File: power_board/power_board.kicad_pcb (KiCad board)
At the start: 2 copper layers, 165.3 x 121.3 mm, 67 parts, among them J1 PROG, J10 M4, J11 5V_1, J12 M5, J13 M6, J14 M7, J15 FAN, J16 Screw_Terminal_01x02, J17 MB_interface, J18 Conn_01x02_Female, J19 12V_1, J2 M1, J20 12V_2, J21 12V_3, J22 12V_4, J23 48V_1, J24 48V_2, J25 48V_3, J26 48V_4, J3 M2, J4 Conn_01x02_Female, J5 Conn_01x02_Female, J6 Conn_01x01_Male, J7 Conn_01x01_Male, J8 Screw_Terminal_01x02, J9 M3, Q1 2N3906, SW1 SW_Push, U1 ACS758xCB-050B-PFF, U2 ACS758xCB-050B-PFF, U3 MCP2515-EST, U4 MAX31855KASA, U5 MCP2551-I-SN, U6 BTS50085-1TMA, U7 ATmega328P-AU, U8 BTS50085-1TMA, U9 LM2596S-5, Y1 20Mhz, Y2 16Mhz

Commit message: silkscreen
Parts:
- added G***: LOGO, title:title, F.Cu at (157.0, 104.5)
- added G***: LOGO, logo:logo, F.Cu at (113.3, 99.8)
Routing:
- net GNDREF: vias 119 -> 118
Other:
- board text added: "- +"
- board text added: "12V-1"
- board text added: "48V-1"
- board text added: "48V-2"
- board text added: "48V-3"
- board text added: "48V-4"
- board text added: "Fan"
- board text added: "M3"
- board text added: "M6"
- board text added: "Motor 1"
- board text added: "Motor 2"
- board text added: "Motor 4"
- board text added: "Motor 5"
- board text added: "Motor 7"
- board text added: "POWER BOARD - REV 1.0"

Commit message: finishing silkscreen
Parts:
- moved R9 1.27 mm to (213.8, 93.6)
- moved C14 0.38 mm to (221.6, 52.5)
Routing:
- net Net-(R9-Pad2): track 1.75 -> 2.49 mm
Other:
- board text added: "12V-2"
- board text added: "12V-3"
- board text added: "12V-4"
- board text added: "5V"
- board text added: "CH"
- board text added: "CL"
- board text added: "Leak Sensors"
- board text added: "TC"
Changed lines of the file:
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@@
   (general
     (thickness 1.6)
-    (drawings 679)
-    (tracks 756)
+    (drawings 688)
+    (tracks 758)
     (zones 0)
     (modules 69)
@@
     (44 Edge.Cuts user)
     (45 Margin user)
-    (46 B.CrtYd user)
-    (47 F.CrtYd user)
+    (46 B.CrtYd user hide)
+    (47 F.CrtYd user hide)
     (48 B.Fab user hide)
     (49 F.Fab user hide)
@@
     (tags resistor)
     (attr smd)
-    (fp_text reference R14 (at 0 1.524 180) (layer F.SilkS)
+    (fp_text reference R14 (at 1.1175 -1.651 180) (layer F.SilkS)
       (effects (font (size 1 1) (thickness 0.15)))
     )
@@
   )
   (module Capacitor_THT:CP_Radial_D7.5mm_P2.50mm (layer F.Cu)
-    (at 221.234 52.451 270)
+    (at 221.615 52.451 270)
     (descr "CP, Radial series, Radial, pin pitch=2.50mm, , diameter=7.5mm, Electrolytic Capacitor")
     (tags "CP Radial series Radial pin pitch 2.50mm  diameter 7.5mm Electrolytic Capacitor")
-    (fp_text reference C14 (at -2.286 4.064) (layer F.SilkS)
+    (fp_text reference C14 (at 5.334 3.429) (layer F.SilkS)
       (effects (font (size 1 1) (thickness 0.15)))
     )
@@
     (tags capacitor)
     (attr smd)
-    (fp_text reference C7 (at 2.159 0.127) (layer F.SilkS)
+    (fp_text reference C7 (at 0.762 -1.905) (layer F.SilkS)
       (effects (font (size 1 1) (thickness 0.15)))
     )
@@
     (descr "CP, Radial series, Radial, pin pitch=7.50mm, , diameter=10mm, Electrolytic Capacitor")
     (tags "CP Radial series Radial pin pitch 7.50mm  diameter 10mm Electrolytic Capacitor")
-    (fp_text reference C2 (at 3.75 -6.25 90) (layer F.SilkS)
+    (fp_text reference C2 (at 8.128 -4.699 180) (layer F.SilkS)
       (effects (font (size 1 1) (thickness 0.15)))
     )
@@
     (tags "SOIC 1.27")
     (attr smd)
-    (fp_text reference U5 (at 2.594092 3.595375) (layer F.SilkS)
+    (fp_text reference U5 (at -2.358908 3.722375) (layer F.SilkS)
       (effects (font (size 1 1) (thickness 0.15)))
     )
@@
     (tags "SOIC 1.27")
     (attr smd)
-    (fp_text reference U4 (at 2.794 3.483) (layer F.SilkS)
+    (fp_text reference U4 (at 1.016 -3.629) (layer F.SilkS)
       (effects (font (size 1 1) (thickness 0.15)))
     )
@@
   )
   (module Resistor_SMD:R_0603_1608Metric (layer F.Cu)
-    (at 215.1125 93.599)
+    (at 213.8425 93.599)
     (descr "Resistor SMD 0603 (1608 Metric), square (rectangular) end terminal, IPC_7351 nominal, (Body size source: http://www.tortai-tech.com/upload/download/2011102023233369053.pdf), generated with kicad-footprint-generator")
     (tags resistor)
@@
     (tags resistor)
     (attr smd)
-    (fp_text reference R8 (at 0 1.397) (layer F.SilkS)
+    (fp_text reference R8 (at 2.667 -0.508) (layer F.SilkS)
       (effects (font (size 1 1) (thickness 0.15)))
     )
@@
     (tags resistor)
     (attr smd)
-    (fp_text reference R2 (at -2.6925 -0.127 180) (layer F.SilkS)
+    (fp_text reference R2 (at 2.54 0.127 180) (layer F.SilkS)
       (effects (font (size 1 1) (thickness 0.15)))
     )
@@
       (xy -0.144472 2.2352) (xy -0.101255 2.253818)) (layer F.SilkS) (width 0.01))
   )
+  (gr_text 5V (at 214.63 67.945 90) (layer F.SilkS)
+    (effects (font (size 1.5 1.5) (thickness 0.375)))
+  )
+  (gr_text "-   +" (at 216.535 64.135 270) (layer F.SilkS)
+    (effects (font (size 1.5 1.5) (thickness 0.375)))
+  )
+  (gr_text TC (at 215.265 79.375 90) (layer F.SilkS)
+    (effects (font (size 1.5 1.5) (thickness 0.375)))
+  )
+  (gr_text CL (at 216.535 101.6 90) (layer F.SilkS)
+    (effects (font (size 1.5 1.5) (thickness 0.375)))
+  )
+  (gr_text CH (at 216.535 92.075 90) (layer F.SilkS)
+    (effects (font (size 1.5 1.5) (thickness 0.375)))
+  )
+  (gr_text "Leak Sensors" (at 200.66 142.24) (layer F.SilkS)
+    (effects (font (size 1.5 1.5) (thickness 0.375)))
+  )
+  (gr_text 12V-4 (at 216.535 49.53) (layer F.SilkS)
+    (effects (font (size 1.5 1.5) (thickness 0.375)))
+  )
+  (gr_text 12V-3 (at 204.47 49.53) (layer F.SilkS)
+    (effects (font (size 1.5 1.5) (thickness 0.375)))
+  )
+  (gr_text 12V-2 (at 191.77 49.53) (layer F.SilkS)
+    (effects (font (size 1.5 1.5) (thickness 0.375)))
+  )
   (gr_text 12V-1 (at 180.34 49.53) (layer F.SilkS)
     (effects (font (size 1.5 1.5) (thickness 0.375)))
@@
     (effects (font (size 1.5 1.5) (thickness 0.375)))
   )
-  (gr_text "Motor 5" (at 131.445 49.53) (layer F.SilkS)
+  (gr_text "Motor 5" (at 132.08 49.53) (layer F.SilkS)
     (effects (font (size 1.5 1.5) (thickness 0.375)))
   )
@@
   (segment (start 196.214199 86.486199) (end 199.514999 86.486199) (width 0.3048) (layer F.Cu) (net 10))
   (segment (start 195.707 85.979) (end 196.214199 86.486199) (width 0.3048) (layer F.Cu) (net 10))
-  (segment (start 215.878908 95.337625) (end 215.878908 93.620092) (width 0.3048) (layer F.Cu) (net 11))
-  (segment (start 215.878908 93.620092) (end 215.9 93.599) (width 0.25) (layer F.Cu) (net 11))
+  (segment (start 215.1675 93.599) (end 215.9 94.3315) (width 0.3048) (layer F.Cu) (net 11))
+  (segment (start 214.63 93.599) (end 215.1675 93.599) (width 0.3048) (layer F.Cu) (net 11))
+  (segment (start 215.9 94.3315) (end 215.9 94.615) (width 0.3048) (layer F.Cu) (net 11))
+  (segment (start 215.9 94.615) (end 215.9 95.25) (width 0.3048) (layer F.Cu) (net 11))
   (segment (start 215.878908 97.877625) (end 219.670625 97.877625) (width 0.3048) (layer F.Cu) (net 12))
   (segment (start 219.670625 97.877625) (end 221.488 99.695) (width 0.3048) (layer F.Cu) (net 12))

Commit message: Finished final Draft of design
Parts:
- Y1: footprint Crystal:Resonator_SMD-3Pin_7.2x3.0mm -> Crystal:Crystal_SMD_0603-2Pin_6.0x3.5mm
- moved C3 8.42 mm to (183.0, 96.3)
- moved C4 6.71 mm to (183.0, 87.1)
- moved G*** 1.57 mm to (114.8, 99.4)
- moved G*** 0.25 mm to (157.0, 104.8)
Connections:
- Y1 pad 1: Net-(C3-Pad2) -> Net-(C4-Pad1)
- Y1 pad 2: Net-(C4-Pad1) -> Net-(C3-Pad2)
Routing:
- net Net-(C3-Pad2): track 0.00 -> 10.9 mm
- net Net-(C4-Pad1): track 0.00 -> 10.2 mm
- net GNDREF: vias 118 -> 119
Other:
- board text added: "GND"
- board text added: "RST"
- board text added: "RX"
- board text added: "TX"

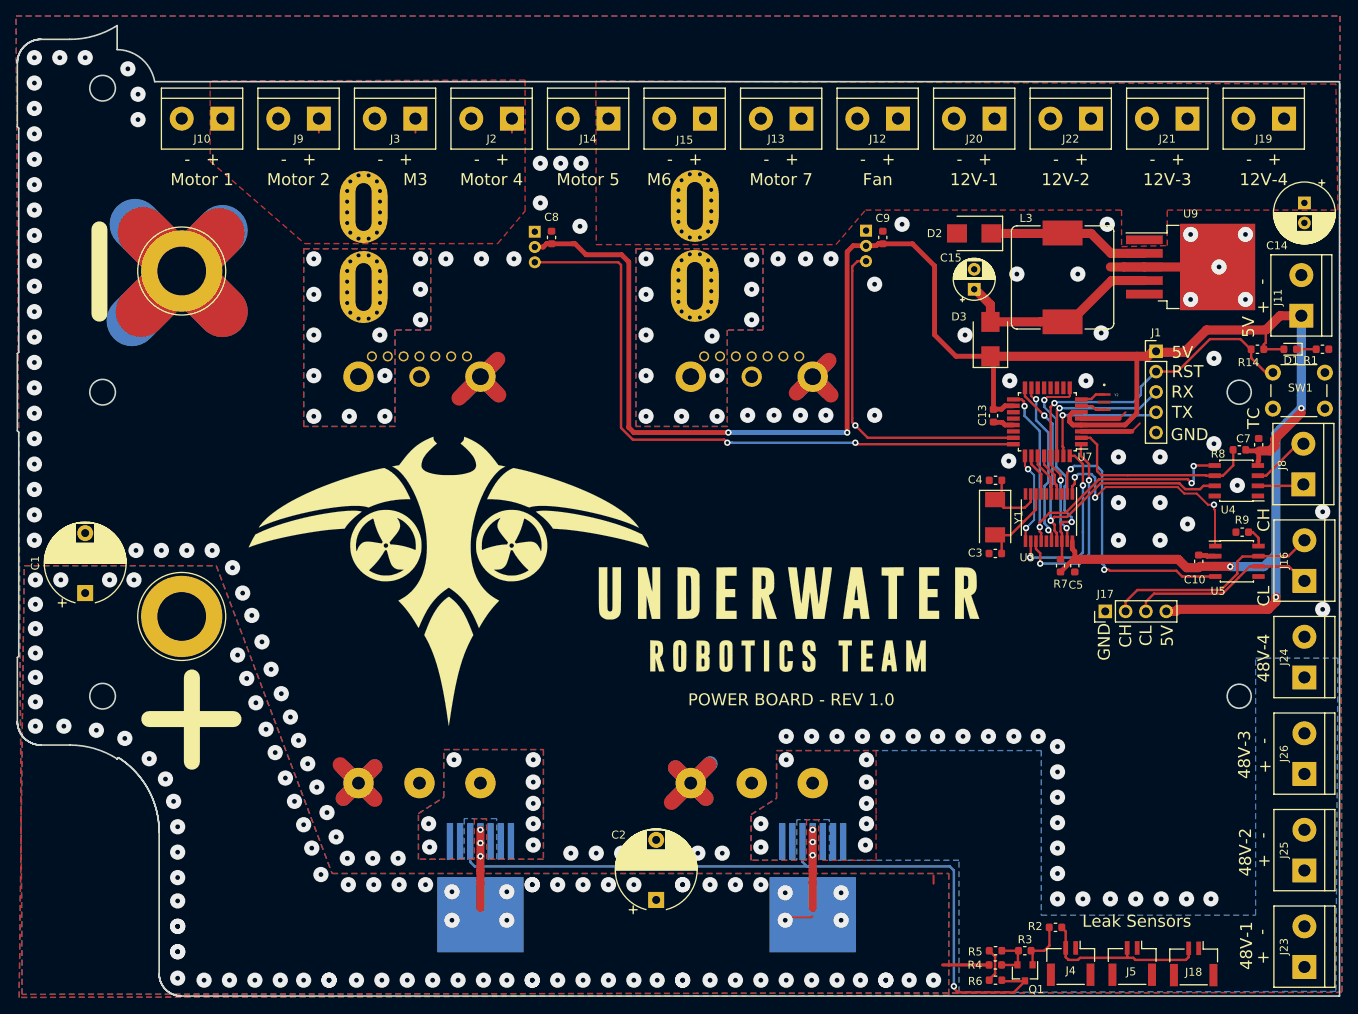
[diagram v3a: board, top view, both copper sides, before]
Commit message: Added fuses
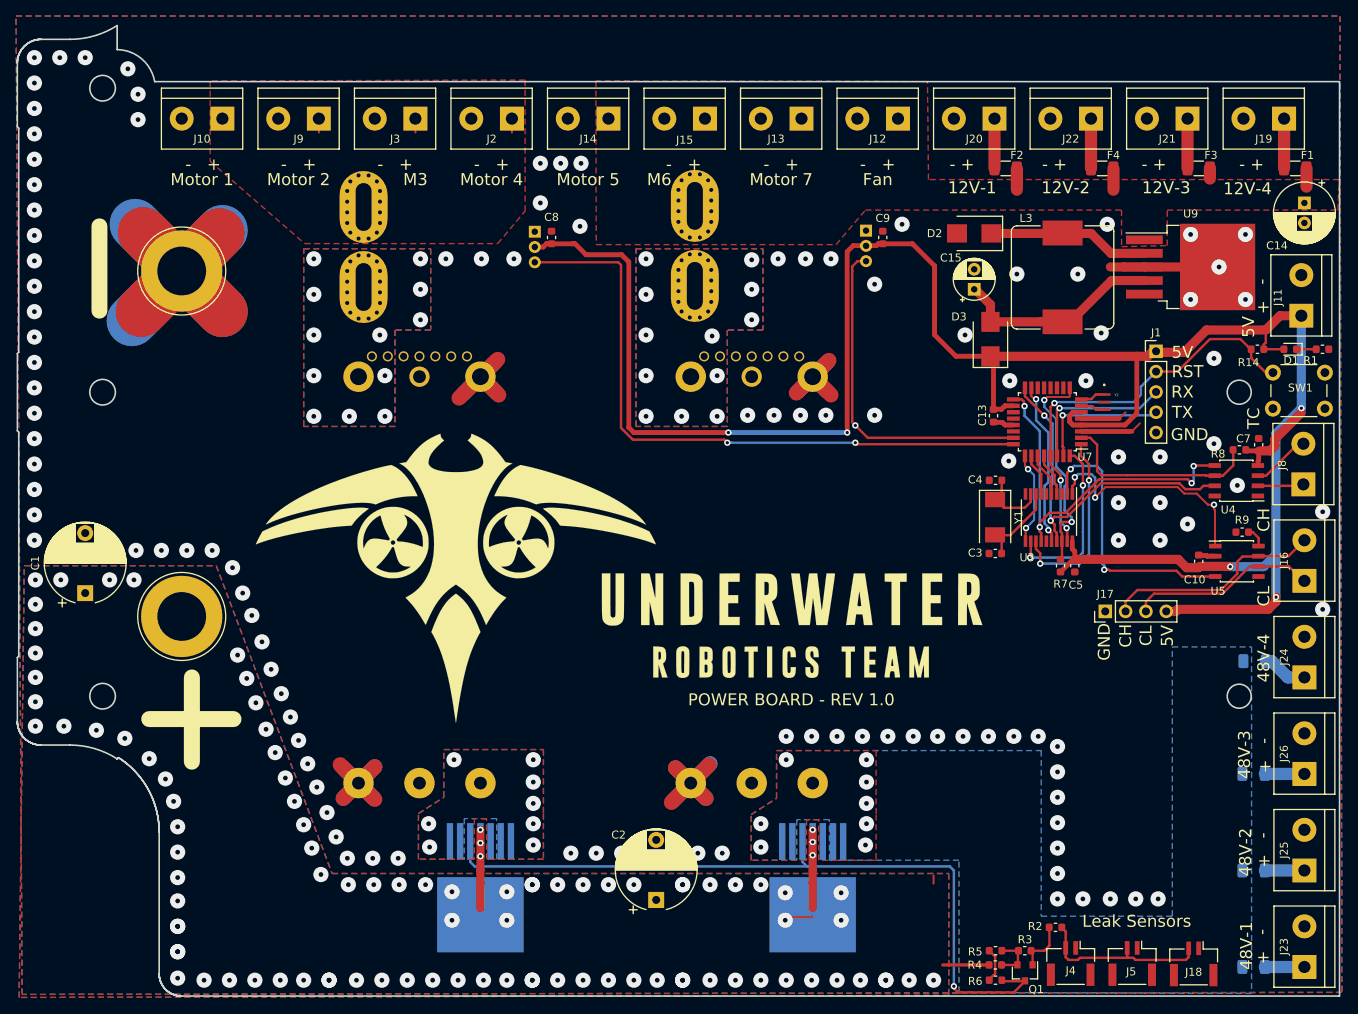
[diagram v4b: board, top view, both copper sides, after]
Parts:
- added F1: Polyfuse_Small, Fuse:Fuse_1206_3216Metric, F.Cu at (220.5, 48.1)
- added F2: Polyfuse_Small, Fuse:Fuse_1206_3216Metric, F.Cu at (184.3, 48.1)
- added F3: Polyfuse_Small, Fuse:Fuse_1206_3216Metric, F.Cu at (208.4, 48.1)
- added F4: Polyfuse_Small, Fuse:Fuse_1206_3216Metric, F.Cu at (196.3, 48.1)
- added F5: Polyfuse_Small, Fuse:Fuse_1206_3216Metric, B.Cu at (215.3, 148.0)
- added F6: Polyfuse_Small, Fuse:Fuse_1206_3216Metric, B.Cu at (215.4, 109.7)
- added F7: Polyfuse_Small, Fuse:Fuse_1206_3216Metric, B.Cu at (215.3, 135.9)
- added F8: Polyfuse_Small, Fuse:Fuse_1206_3216Metric, B.Cu at (215.3, 123.8)
- moved G*** 0.97 mm to (115.7, 99.1)
- moved G*** 0.85 mm to (157.4, 105.5)
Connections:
- J19 pad 1: +12VA -> Net-(F1-Pad1)
- J20 pad 1: +12VA -> Net-(F2-Pad1)
- J21 pad 1: +12VA -> Net-(F3-Pad1)
- J22 pad 1: +12VA -> Net-(F4-Pad1)
- J23 pad 1: 48V -> Net-(F5-Pad2)
- J24 pad 1: 48V -> Net-(F6-Pad2)
- J25 pad 1: 48V -> Net-(F7-Pad2)
- J26 pad 1: 48V -> Net-(F8-Pad2)
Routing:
- net +12VA: track 0.00 -> 9.11 mm
- net Net-(F2-Pad1): track 0.00 -> 6.22 mm
- net Net-(F1-Pad1): track 0.00 -> 6.22 mm
- net Net-(F4-Pad1): track 0.00 -> 6.09 mm
- net Net-(F3-Pad1): track 0.00 -> 6.09 mm
- net Net-(F6-Pad2): track 0.00 -> 5.53 mm
- net Net-(F7-Pad2): track 0.00 -> 5.00 mm
- net Net-(F5-Pad2): track 0.00 -> 4.82 mm
- net Net-(F8-Pad2): track 0.00 -> 4.82 mm
- net GNDREF: vias 119 -> 117

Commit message: updated outline, added 3d file for ben
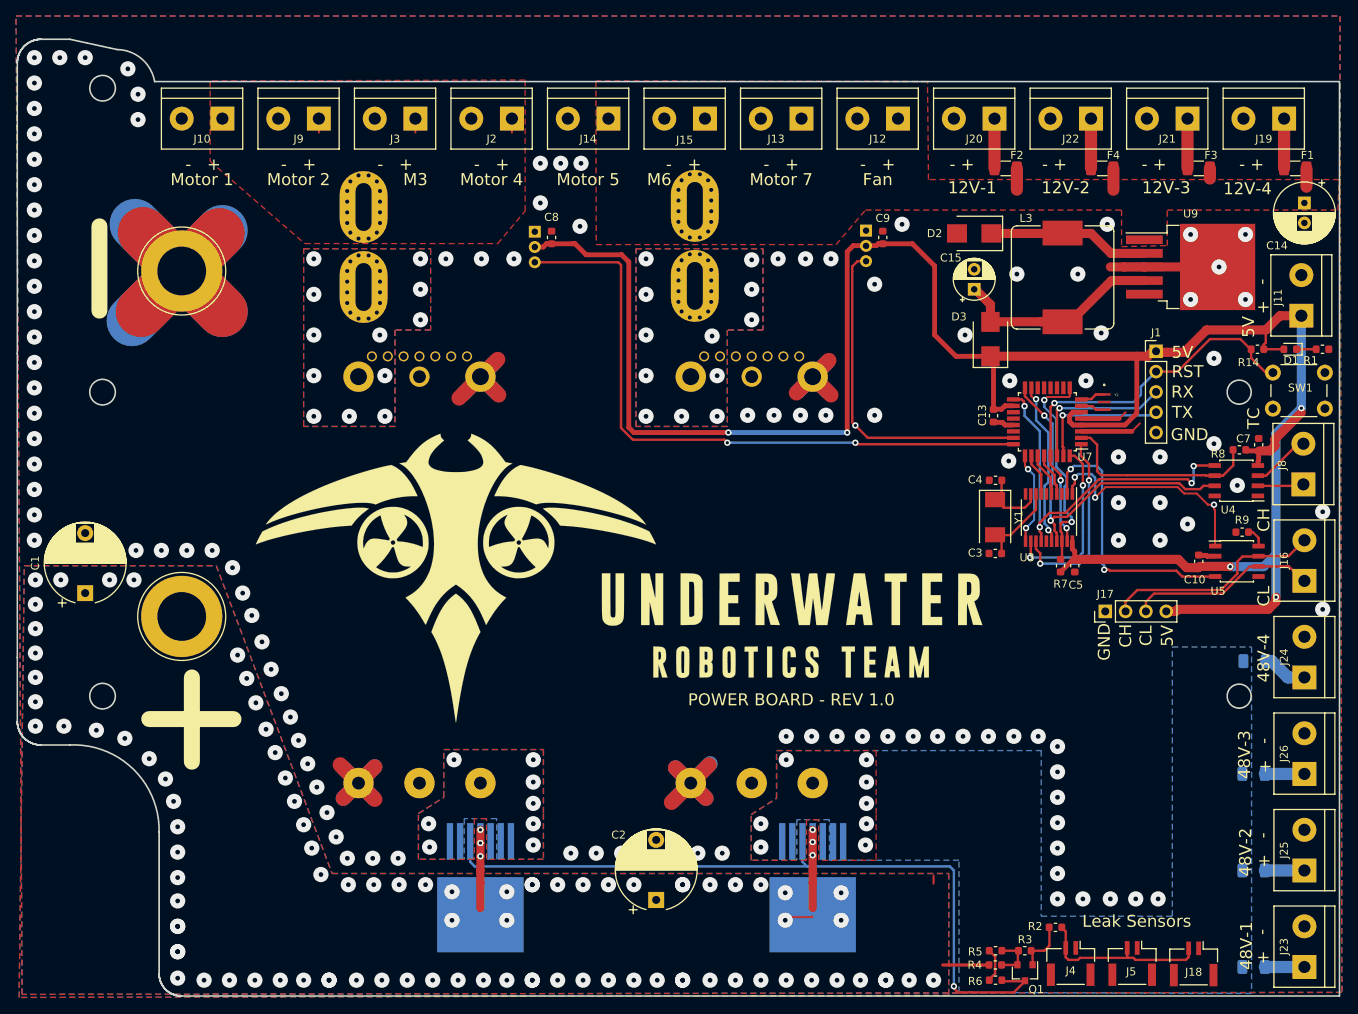
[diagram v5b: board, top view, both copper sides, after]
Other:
- board size 165.3 x 121.3 mm -> 165.3 x 119.6 mm

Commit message: post-board review edits
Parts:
- removed D3: --, Diode_SMD:D_SMB
- removed G***: LOGO, logo:logo
- removed G***: LOGO, title:title
- added C6: 0.1uF, Capacitor_SMD:C_0603_1608Metric, F.Cu at (213.7, 75.0)
- added J27: Screw_Terminal_01x02, Connector_PinHeader_2.54mm:PinHeader_1x02_P2.54mm_Vertical, F.Cu at (221.6, 84.8)
- added R10: 10k, Resistor_SMD:R_0603_1608Metric, F.Cu at (211.3, 75.7)
- added U10: MAX31855KASA, Package_SO:SOIC-8_3.9x4.9mm_P1.27mm, F.Cu at (211.0, 79.4)
- J8: footprint TerminalBlock:TerminalBlock_bornier-2_P5.08mm -> Connector_PinHeader_2.54mm:PinHeader_1x02_P2.54mm_Vertical
- moved J1 10.5 mm to (200.0, 81.0), turned to 180 degrees
- moved J8 2.42 mm to (221.6, 90.0), turned to 180 degrees
- moved C7 2.33 mm to (213.9, 83.8)
- moved R8 2.33 mm to (211.5, 84.5)
- moved U4 2.33 mm to (211.1, 88.3)
- moved C10 2.16 mm to (206.2, 97.3)
- moved U5 2.16 mm to (211.0, 97.2)
- moved R9 0.90 mm to (213.0, 93.5)
- moved J17 0.25 mm to (196.7, 103.3)
- turned C8 to 270 degrees
- turned C9 to 270 degrees
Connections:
- net TC_CS renamed TC1_CS
- C15 pad 1: Net-(C15-Pad1) -> +5V
- J1 pad 1: +5V -> GNDREF
- J1 pad 2: RESET -> TX
- J1 pad 4: TX -> RESET
- J1 pad 5: GNDREF -> +5V
- L3 pad 2: Net-(C15-Pad1) -> +5V
- U1 pad 1: GNDREF -> +5V
- U1 pad 2: +5V -> GNDREF
- U2 pad 1: GNDREF -> +5V
- U2 pad 2: +5V -> GNDREF
- U7 pad 10: Net-(U7-Pad10) -> TC2_CS
- U9 pad 4: Net-(C15-Pad1) -> +5V
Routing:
- net TC2_CS: track 0.00 -> 42.1 mm, vias 0 -> 4
- net +5V: track 281.3 -> 311.0 mm, vias 5 -> 9
- net Net-(C15-Pad1): track 26.5 -> 0.00 mm
- net Net-(J27-Pad1): track 0.00 -> 9.93 mm
- net Net-(J27-Pad2): track 0.00 -> 9.41 mm
- net SCK: track 46.7 -> 54.8 mm, vias 4 -> 5
- net MISO: track 43.9 -> 51.3 mm, vias 2 -> 4
- net RESET: track 51.9 -> 57.1 mm
- net RX: track 19.1 -> 15.8 mm
- net TX: track 16.9 -> 13.7 mm
- net CAN_RX: track 34.3 -> 31.7 mm
- net Net-(J8-Pad1): track 5.76 -> 8.29 mm
- net CANH: track 27.6 -> 26.0 mm
- net TC1_CS: track 25.4 -> 23.8 mm
- net CAN_TX: track 29.0 -> 28.0 mm, vias 3 -> 2
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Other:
- outline, holes or cut-outs redrawn
- net class Default: trace_width 0.25 -> 0.3048
- board text removed: "TC"
